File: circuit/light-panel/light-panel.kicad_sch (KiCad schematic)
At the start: 32 parts, among them J1 Screw_Terminal_01x02

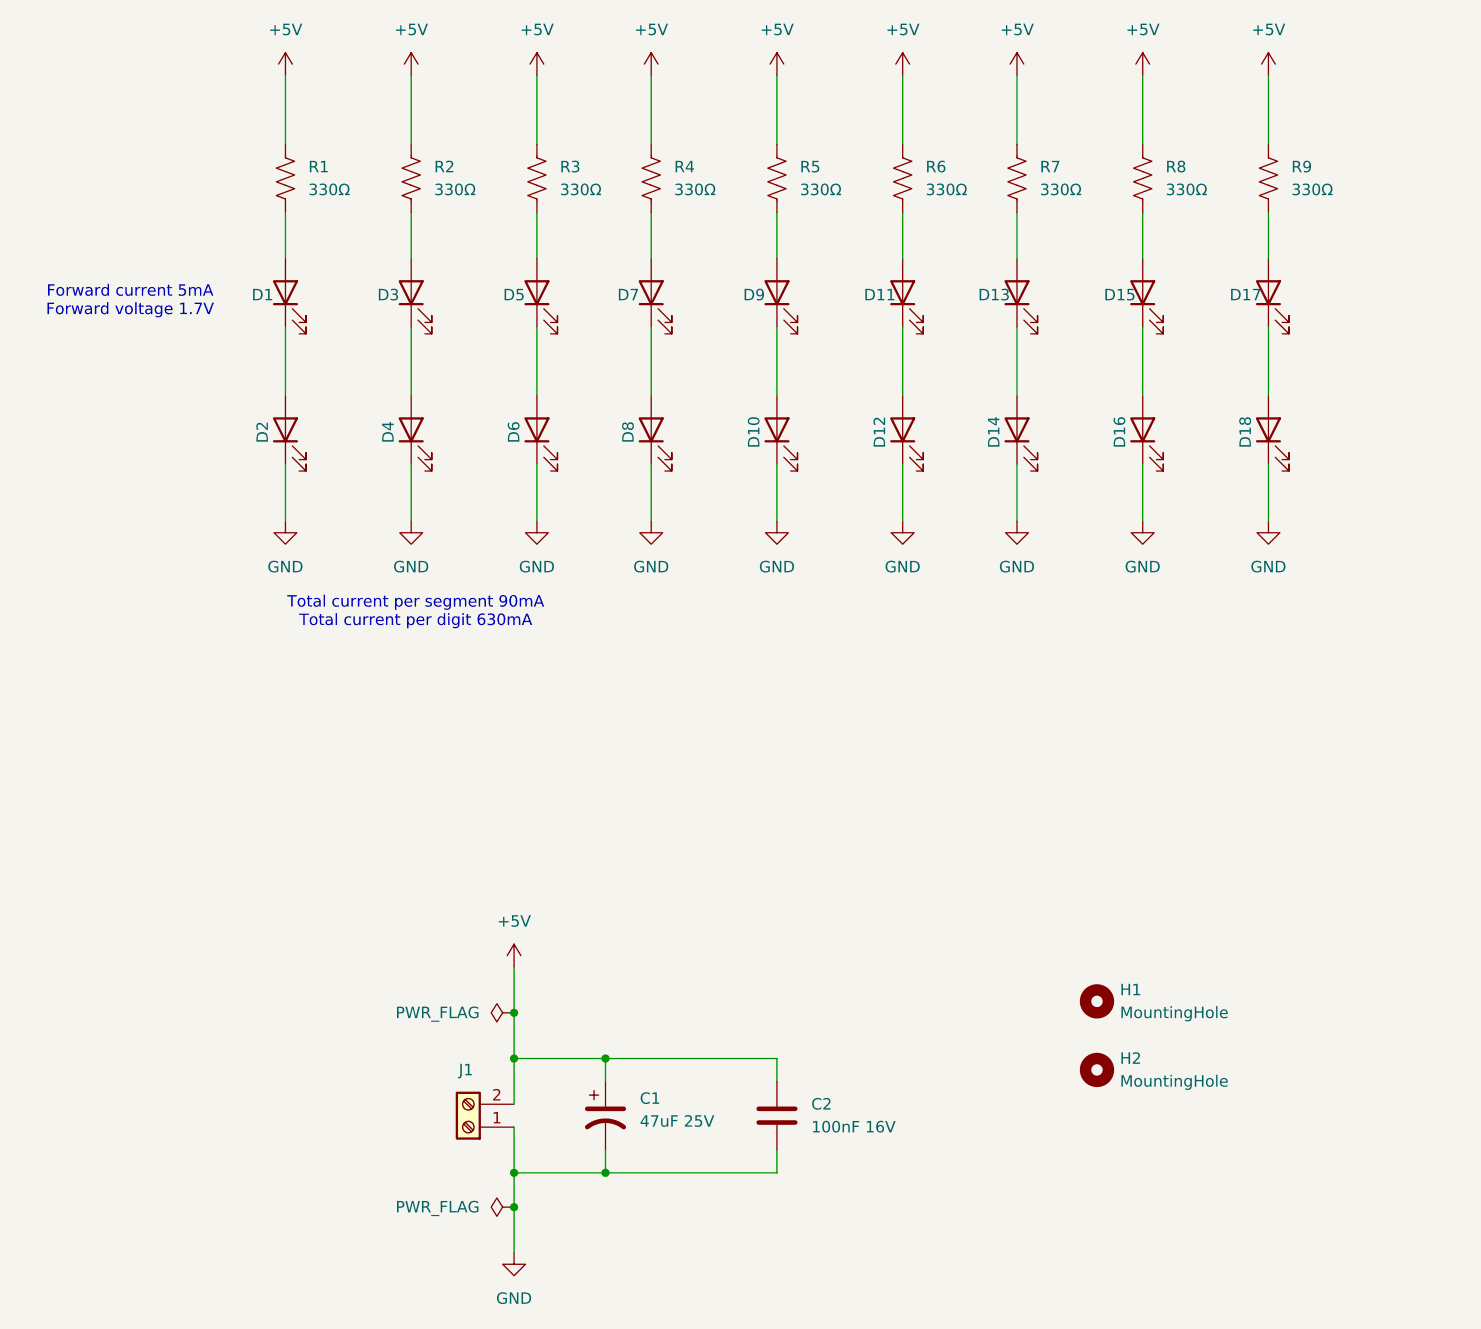
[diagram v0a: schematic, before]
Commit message: rearrage leds
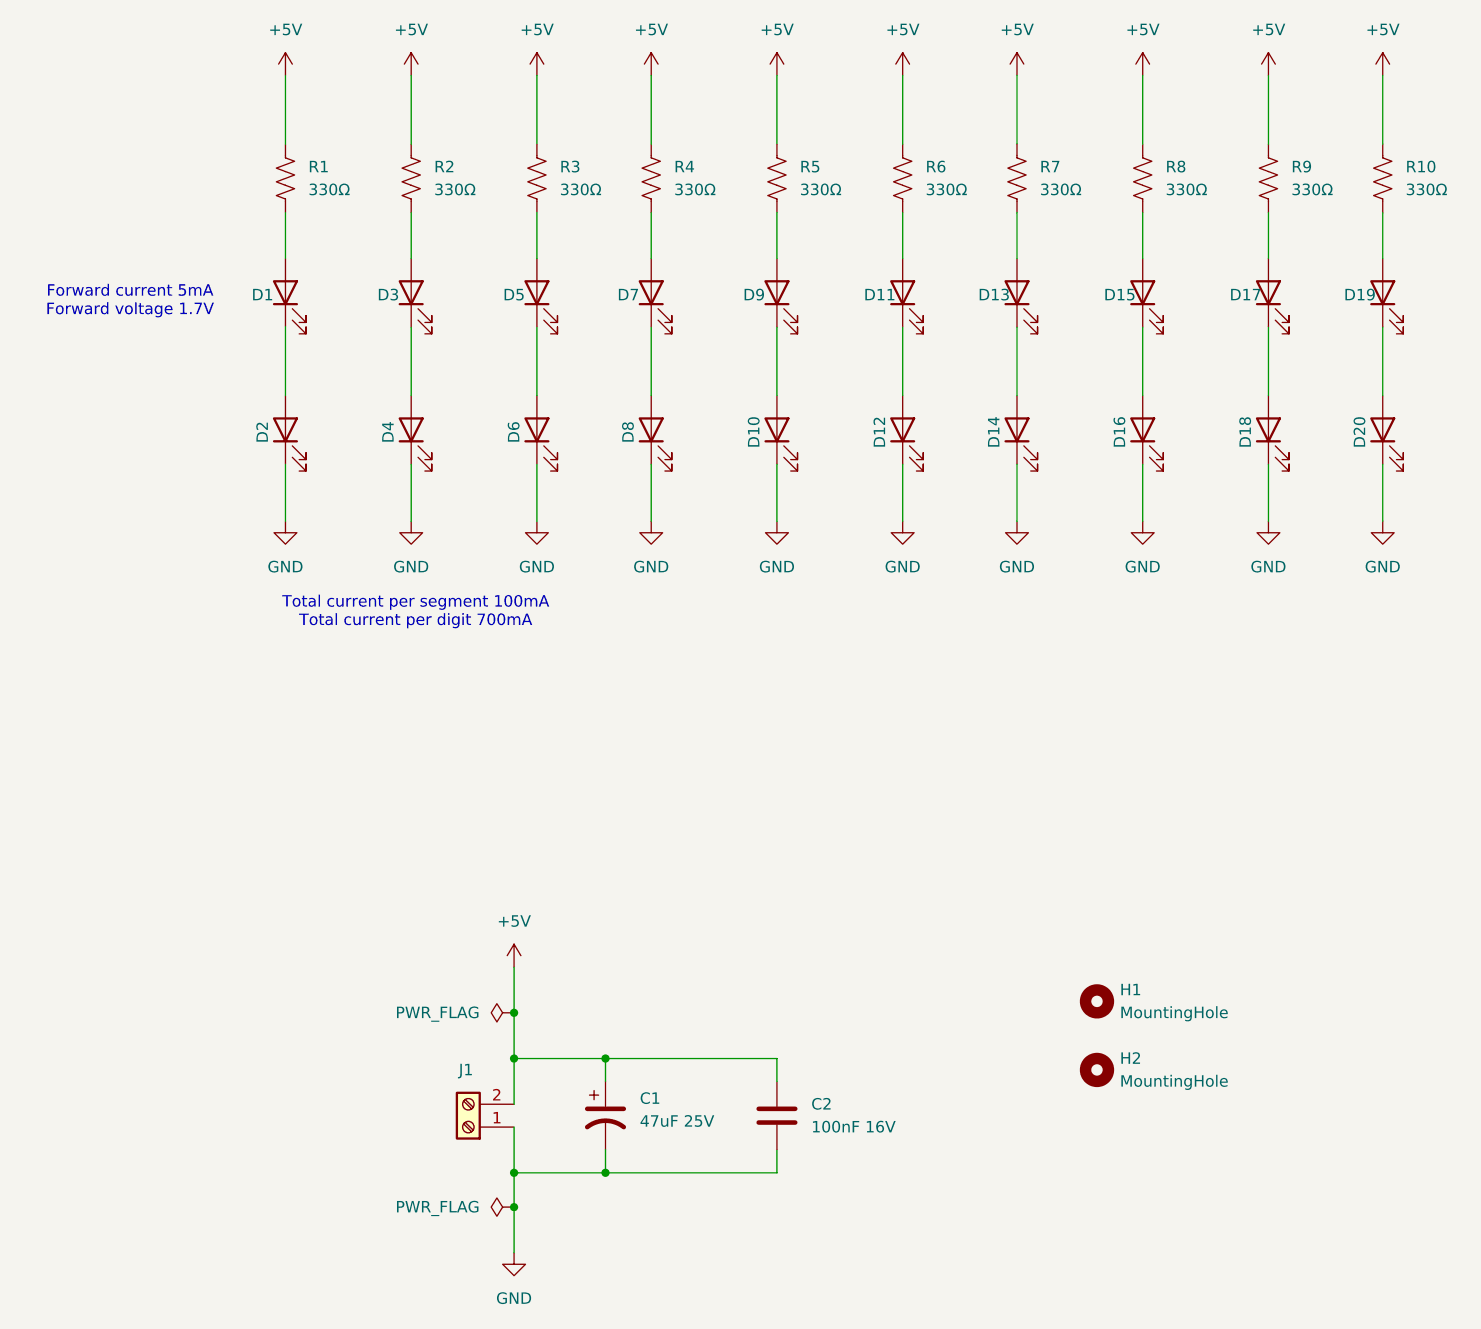
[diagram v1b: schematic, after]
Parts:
- added D19, D20: KT-0603R, LED_SMD:LED_0603_1608Metric, symbol Device:LED
- added R10: 330Ω, Resistor_SMD:R_0603_1608Metric, symbol Device:R_US
- J1: now left out of the parts list
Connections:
- net +5V: now also R10.1
- net GND: now also D20.1 (K)
- new net: D19.2 (A), R10.2
- new net: D19.1 (K), D20.2 (A)
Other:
- note added: "Total current per segment 100mA Total current per digit 700mA"
- note removed: "Total current per segment 90mA Total current per digit 630mA"
